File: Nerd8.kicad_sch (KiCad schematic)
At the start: 3 parts, among them J1 Conn_01x04

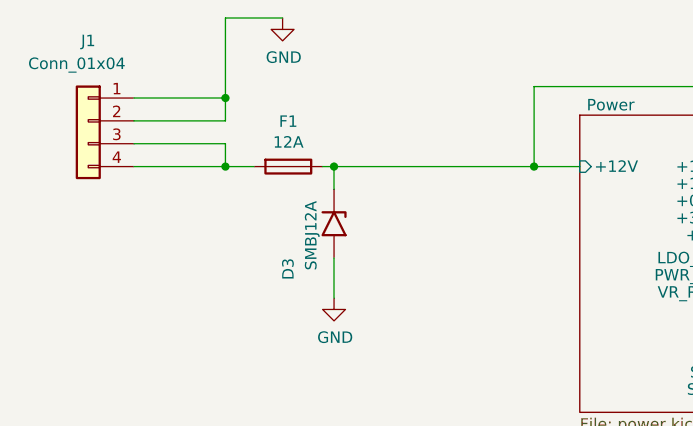
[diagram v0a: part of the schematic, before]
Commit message: Changed Fuse to 10A with Fuseholder
Fuse in Bom with FuseHolder
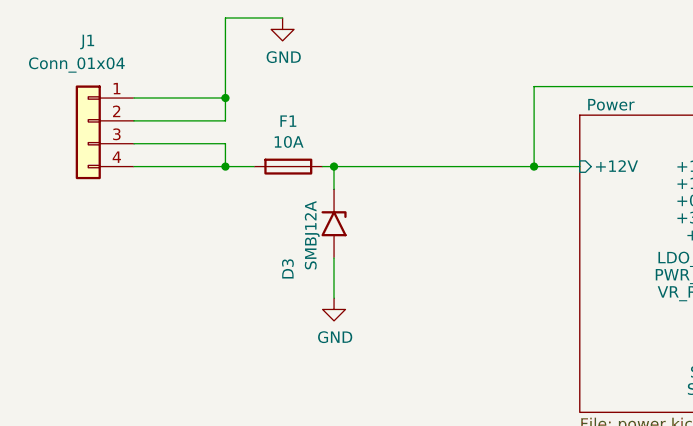
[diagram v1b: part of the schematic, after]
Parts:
- F1: value 12A -> 10A; Manufacturer 0451012.MRL -> 0154010.DR; OrderNr F2592CT-ND -> F1251CT-ND
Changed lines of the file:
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@@
 			)
 		)
-		(property "Value" "12A"
+		(property "Value" "10A"
 			(at 50.165 49.3776 90)
 			(effects
@@
 			)
 		)
-		(property "Manufacturer" "0451012.MRL"
+		(property "Manufacturer" "0154010.DR"
 			(at 50.165 52.07 0)
 			(effects
@@
 			)
 		)
-		(property "OrderNr" "F2592CT-ND"
+		(property "OrderNr" "F1251CT-ND"
 			(at 50.165 52.07 0)
 			(effects
